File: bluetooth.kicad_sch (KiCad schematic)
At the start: 1 part, among them U1 RNBD451PE-I100

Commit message: still initial layout
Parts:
- added C1, C3: 4.7uF 10V, Capacitor_SMD:C_0603_1608Metric, symbol Device:C_Small
- added C2, C4: 0.1uF 10V, Capacitor_SMD:C_0402_1005Metric, symbol Device:C_Small
- added D1: GREEN, LED_SMD:LED_0402_1005Metric, symbol Device:LED_Small
- added D2: BLUE, LED_SMD:LED_0402_1005Metric, symbol Device:LED_Small
- added D3: RED, LED_SMD:LED_0402_1005Metric, symbol Device:LED_Small
- added J2: Conn_01x03_Pin, Connector_PinHeader_2.54mm:PinHeader_1x03_P2.54mm_Vertical, symbol Connector:Conn_01x03_Pin
- added R10, R8, R9: 470, Resistor_SMD:R_0402_1005Metric, symbol Device:R_Small
- added R7: 0, Resistor_SMD:R_0402_1005Metric, symbol Device:R_Small
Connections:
- net GND: now also C1.1, C2.1, C3.1, C4.1, D1.1 (K), J2.1 (Pin_1)
- net 3V3_VDD_BT: now reaches U1.27 (VDD)
- net 3V3_VDD_BT: now also U1.28 (VDD), U1.7 (VDD_A), C1.2, C2.2, C3.2, C4.2, R7.1
- net DEBUG_TX: now reaches U1.29 (PA8)
- net DEBUG_TX: now also J2.3 (Pin_3)
- net DEBUG_RX: now reaches U1.31 (PA7)
- net DEBUG_RX: now also J2.2 (Pin_2)
- net at U1.36 (PA3): now also D3.1 (K)
- net at U1.6 (PB5): now also D2.1 (K)
- new net: D1.2 (A), R8.1
- new net: D2.2 (A), R9.2
- new net: D3.2 (A), R10.2
- new net +3V3SW: R10.1, R7.2, R8.2, R9.1

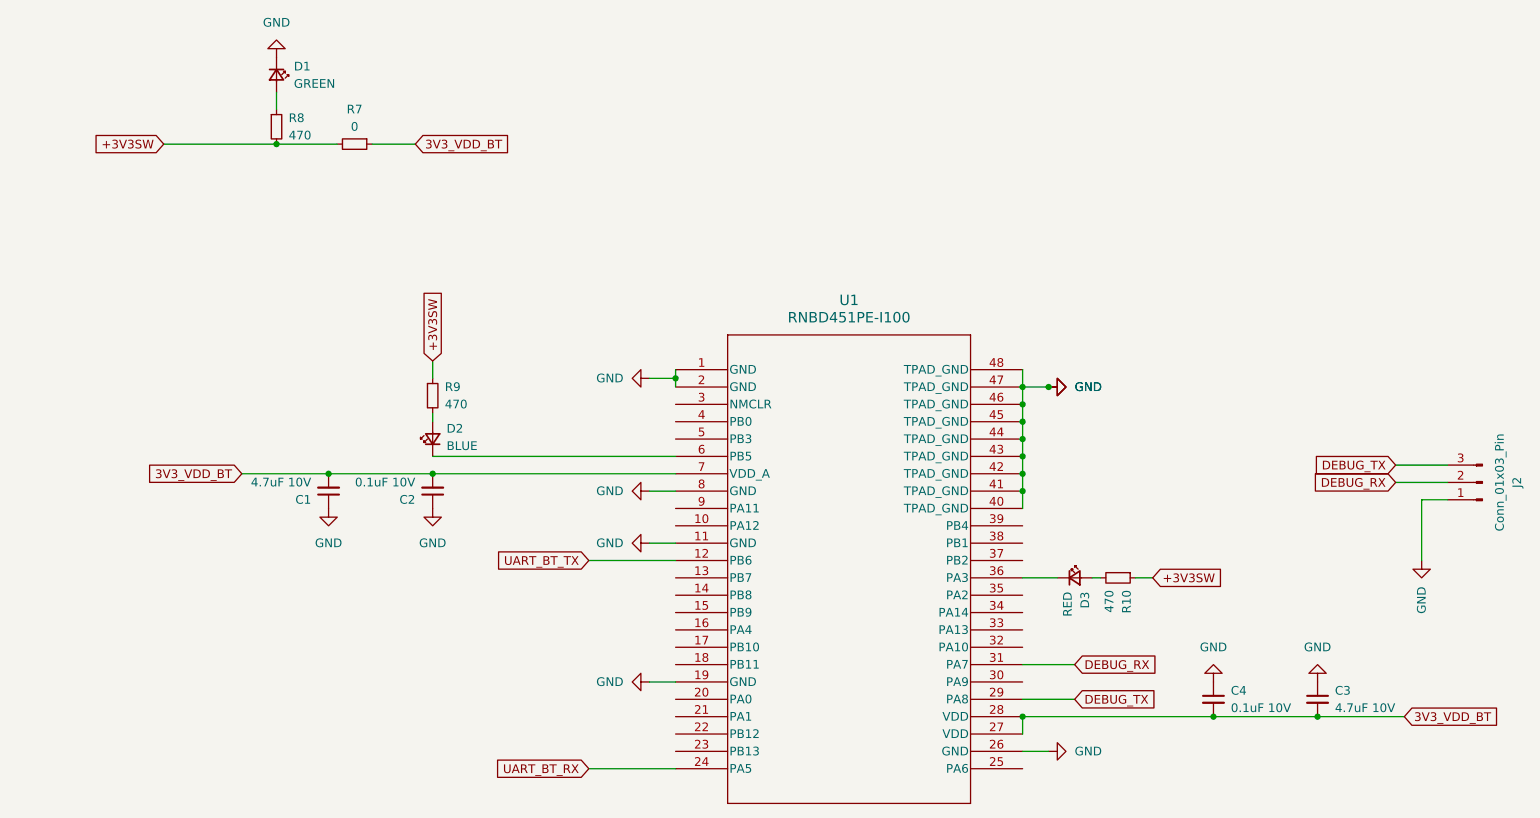
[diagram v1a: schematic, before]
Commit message: igntion igbt, cooling mosfet
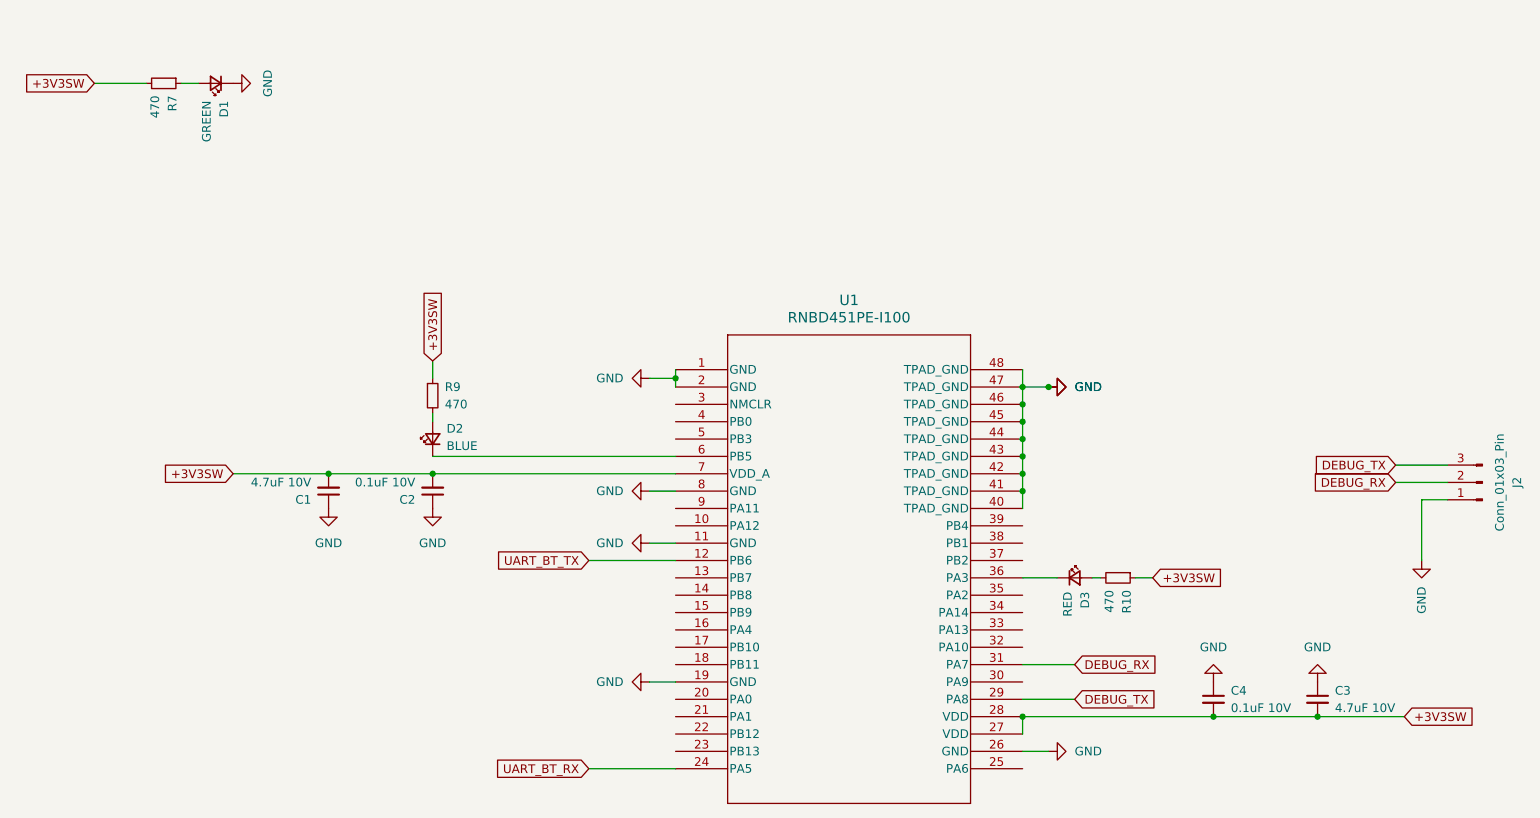
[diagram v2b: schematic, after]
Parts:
- removed R8: 470, Resistor_SMD:R_0402_1005Metric, symbol Device:R_Small
- R7: value 0 -> 470
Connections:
- net +3V3SW: now also C1.2, C2.2, C3.2, C4.2, U1.27 (VDD), U1.28 (VDD), U1.7 (VDD_A)
- net at D1.2 (A): now also R7.1
- removed net 3V3_VDD_BT: C1.2, C2.2, C3.2, C4.2, R7.1, U1.27 (VDD), U1.28 (VDD), U1.7 (VDD_A)

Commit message: large cap, more silkscreen for big connector
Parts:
- U1: footprint footprints:MOD39_15p5X20p7X2p8_ZSX_MCH -> RNBD451PE:MOD39_15p5X20p7X2p8_ZSX_MCH
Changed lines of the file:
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@@
 			)
 		)
-		(property "Footprint" "footprints:MOD39_15p5X20p7X2p8_ZSX_MCH"
+		(property "Footprint" "RNBD451PE:MOD39_15p5X20p7X2p8_ZSX_MCH"
 			(at 116.84 64.77 0)
 			(effects

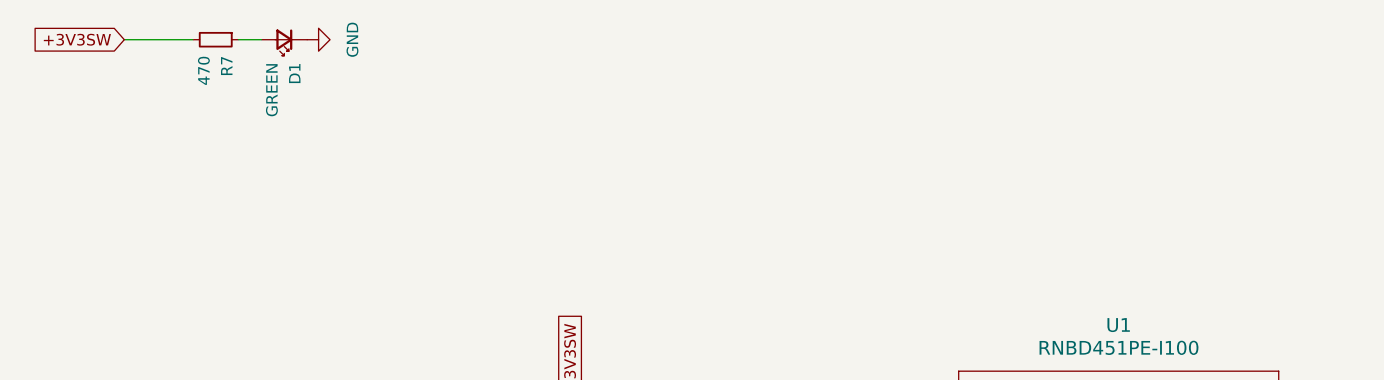
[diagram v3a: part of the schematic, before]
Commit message: update main connector footprint
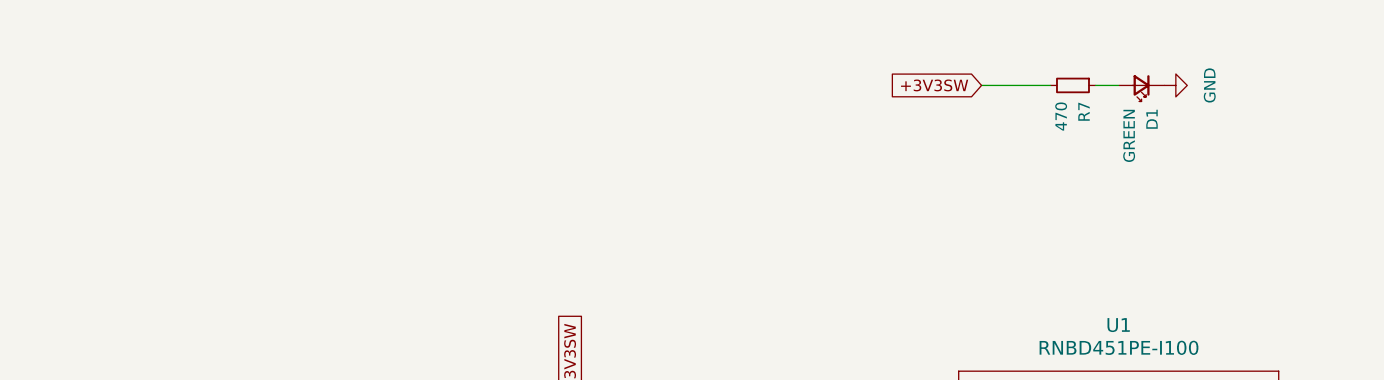
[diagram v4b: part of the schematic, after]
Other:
- moved on the sheet: D1, R7
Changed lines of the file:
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@@
 	(wire
 		(pts
-			(xy 31.75 22.86) (xy 39.37 22.86)
+			(xy 127 27.94) (xy 134.62 27.94)
 		)
 		(stroke
@@
 	(wire
 		(pts
-			(xy 46.99 22.86) (xy 44.45 22.86)
+			(xy 142.24 27.94) (xy 139.7 27.94)
 		)
 		(stroke
@@
 	(global_label "+3V3SW"
 		(shape input)
-		(at 31.75 22.86 180)
+		(at 127 27.94 180)
 		(fields_autoplaced yes)
 		(effects
@@
 		)
 		(property "Intersheetrefs" "${INTERSHEET_REFS}"
-			(at 21.0239 22.86 0)
+			(at 116.2739 27.94 0)
 			(effects
 				(font
@@
 	(symbol
 		(lib_id "Device:LED_Small")
-		(at 49.53 22.86 180)
+		(at 144.78 27.94 180)
 		(unit 1)
 		(exclude_from_sim no)
@@
 		(fields_autoplaced yes)
 		(property "Reference" "D1"
-			(at 50.7366 25.4 90)
+			(at 145.9866 30.48 90)
 			(effects
 				(font
@@
 		)
 		(property "Value" "GREEN"
-			(at 48.1966 25.4 90)
+			(at 143.4466 30.48 90)
 			(effects
 				(font
@@
 		)
 		(property "Footprint" "LED_SMD:LED_0402_1005Metric"
-			(at 49.53 22.86 90)
+			(at 144.78 27.94 90)
 			(effects
 				(font
@@
 		)
 		(property "Datasheet" "~"
-			(at 49.53 22.86 90)
+			(at 144.78 27.94 90)
 			(effects
 				(font
@@
 		)
 		(property "Description" "Light emitting diode, small symbol"
-			(at 49.53 22.86 0)
+			(at 144.78 27.94 0)
 			(effects
 				(font
@@
 	(symbol
 		(lib_id "Device:R_Small")
-		(at 41.91 22.86 270)
+		(at 137.16 27.94 270)
 		(unit 1)
 		(exclude_from_sim no)
@@
 		(dnp no)
 		(property "Reference" "R7"
-			(at 43.18 24.638 0)
+			(at 138.43 29.718 0)
 			(effects
 				(font
@@
 		)
 		(property "Value" "470"
-			(at 40.64 24.638 0)
+			(at 135.89 29.718 0)
 			(effects
 				(font
@@
 		)
 		(property "Footprint" "Resistor_SMD:R_0402_1005Metric"
-			(at 41.91 22.86 0)
+			(at 137.16 27.94 0)
 			(effects
 				(font
@@
 		)
 		(property "Datasheet" "~"
-			(at 41.91 22.86 0)
+			(at 137.16 27.94 0)
 			(effects
 				(font
@@
 		)
 		(property "Description" "Resistor, small symbol"
-			(at 41.91 22.86 0)
+			(at 137.16 27.94 0)
 			(effects
 				(font
@@
 	(symbol
 		(lib_id "power:GND")
-		(at 52.07 22.86 90)
+		(at 147.32 27.94 90)
 		(unit 1)
 		(exclude_from_sim no)
@@
 		(fields_autoplaced yes)
 		(property "Reference" "#PWR033"
-			(at 58.42 22.86 0)
+			(at 153.67 27.94 0)
 			(effects
 				(font
@@
 		)
 		(property "Value" "GND"
-			(at 57.15 22.86 0)
+			(at 152.4 27.94 0)
 			(effects
 				(font
@@
 		)
 		(property "Footprint" ""
-			(at 52.07 22.86 0)
+			(at 147.32 27.94 0)
 			(effects
 				(font
@@
 		)
 		(property "Datasheet" ""
-			(at 52.07 22.86 0)
+			(at 147.32 27.94 0)
 			(effects
 				(font
@@
 		)
 		(property "Description" "Power symbol creates a global label with name \"GND\" , ground"
-			(at 52.07 22.86 0)
-			(effects
-				(font
+			(at 147.32 27.94 0)
+			(effects
+				(font
